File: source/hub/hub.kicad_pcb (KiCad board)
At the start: 2 copper layers, 72 x 15 mm, 18 parts, among them J1 10.0 180° ZCJB-HJ, J2 10.0 180° ZCJB-HJ, J3 918-118A2021Y40002, J4 TYPEC-303-ACP16, U1 SL2.1A, X1 12 MHz

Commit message: finished redesigning
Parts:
- C3: value 10uF -> 10 uF
- moved X1 0.25 mm to (202.7, 100.5)
- moved R2 0.10 mm to (160.3, 106.9)
- renumbered J2 to J1, J3 to J2, J1 to J3
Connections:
- J1 pad 2: /DM2 -> /DM1
- J1 pad 3: /DP2 -> /DP1
- J3 pad 2: /DM1 -> /DM2
- J3 pad 3: /DP1 -> /DP2
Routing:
- net /DP2: track 35.6 -> 15.2 mm, vias 1 -> 0
- net /DM: track 43.1 -> 62.8 mm, vias 0 -> 3
- net /DM3: track 36.6 -> 54.2 mm, vias 1 -> 2
- net /DP1: track 12.1 -> 29.6 mm
- net /DM1: track 14.1 -> 29.8 mm
- net /DP: track 46.3 -> 60.3 mm
- net /DP3: track 40.7 -> 53.0 mm, vias 3 -> 2
- net /DM2: track 25.6 -> 16.7 mm
- net Net-(C7-Pad1): track 21.4 -> 16.1 mm, vias 1 -> 2
- net +5V: track 86.1 -> 84.6 mm, vias 3 -> 4
- net Earth: track 113.2 -> 114.6 mm, vias 0 -> 6
- net Net-(U1-VDD18): track 2.99 -> 3.57 mm
- net Net-(U1-XOUT): track 14.4 -> 13.9 mm, vias 2 -> 0

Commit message: updated missing routes
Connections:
- C7 pad 1: Net-(C7-Pad1) -> +5V
- C8 pad 1: Net-(C7-Pad1) -> +5V
- J2 pad 10: Net-(C7-Pad1) -> +5V
- J2 pad 15: Net-(C7-Pad1) -> +5V
- J2 pad 2: Net-(C7-Pad1) -> +5V
- J2 pad 7: Net-(C7-Pad1) -> +5V
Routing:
- net +5V: track 84.6 -> 114.9 mm, vias 4 -> 7
- net Net-(C7-Pad1): track 16.1 -> 0.00 mm, vias 2 -> 0

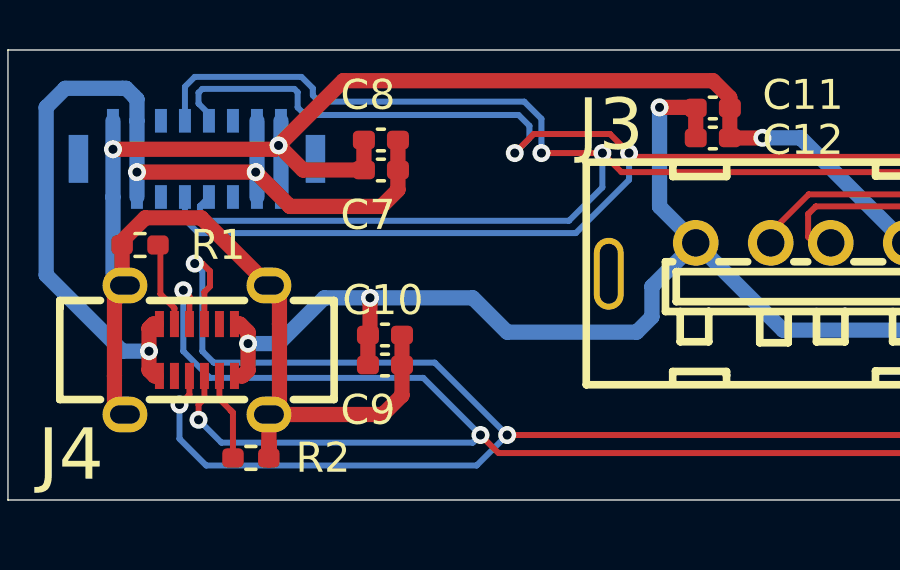
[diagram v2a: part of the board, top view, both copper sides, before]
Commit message: add name and contact
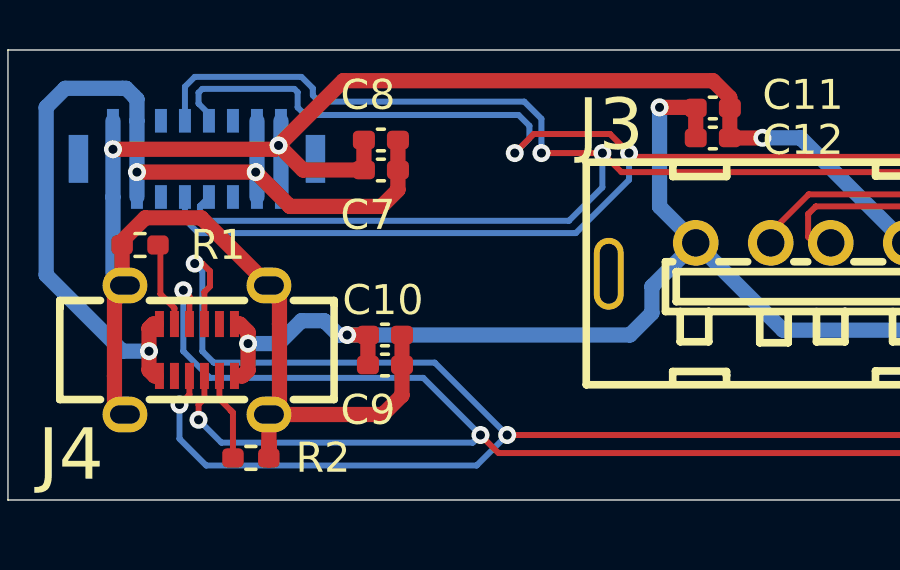
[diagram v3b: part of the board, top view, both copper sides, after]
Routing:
- net +5V: track 114.9 -> 113.7 mm
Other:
- board text added: "Designed By Ethan Hu 4/14/2025"
- board text added: "Email: ethanhu8351@gmail.com Github: PythonOrC"
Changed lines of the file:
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@@
 		(layer "Edge.Cuts")
+	)
+	(gr_text "Designed By Ethan Hu 4/14/2025"
+		(at 222.283075 97.2231 0)
+		(layer "B.SilkS")
+		(effects
+			(font
+				(size 1.5 1.5)
+				(thickness 0.3)
+				(bold yes)
+			)
+			(justify left bottom mirror)
+		)
+	)
+	(gr_text "Email: ethanhu8351@gmail.com\nGithub: PythonOrC"
+		(at 222.283075 106.3671 0)
+		(layer "B.SilkS")
+		(effects
+			(font
+				(size 1.143 1.143)
+				(thickness 0.2286)
+				(bold yes)
+			)
+			(justify left bottom mirror)
+		)
 	)
 	(segment
@@
 	)
 	(segment
-		(start 164.244075 101.5411)
-		(end 164.244075 102.711125)
-		(width 0.508)
-		(layer "F.Cu")
-		(net 2)
-	)
-	(segment
 		(start 160.180075 103.0651)
 		(end 160.180075 102.6841)
@@
 	)
 	(segment
-		(start 164.244075 102.711125)
-		(end 164.1761 102.7791)
-		(width 0.508)
-		(layer "F.Cu")
-		(net 2)
-	)
-	(segment
 		(start 159.989955 104.14422)
 		(end 159.83016 104.14422)
@@
 	)
 	(segment
+		(start 163.482075 102.7791)
+		(end 164.1761 102.7791)
+		(width 0.508)
+		(layer "F.Cu")
+		(net 2)
+	)
+	(segment
 		(start 198.788075 106.7481)
 		(end 198.788075 103.1921)
@@
 	)
 	(via
-		(at 164.244075 101.5411)
+		(at 163.482075 102.7791)
 		(size 0.6)
 		(drill 0.3)
@@
 	)
 	(segment
+		(start 161.196075 103.0651)
+		(end 160.180075 103.0651)
+		(width 0.508)
+		(layer "B.Cu")
+		(net 2)
+	)
+	(segment
 		(start 156.370075 94.8101)
 		(end 156.116075 94.5561)
@@
 	)
 	(segment
+		(start 163.482075 102.7791)
+		(end 172.912075 102.7791)
+		(width 0.508)
+		(layer "B.Cu")
+		(net 2)
+	)
+	(segment
 		(start 154.084075 94.5561)
 		(end 153.449075 95.1911)
@@
 	)
 	(segment
+		(start 162.720075 102.3031)
+		(end 161.958075 102.3031)
+		(width 0.508)
+		(layer "B.Cu")
+		(net 2)
+	)
+	(segment
+		(start 173.642075 101.1601)
+		(end 175.094215 99.70796)
+		(width 0.508)
+		(layer "B.Cu")
+		(net 2)
+	)
+	(segment
+		(start 172.912075 102.7791)
+		(end 173.642075 102.0491)
+		(width 0.508)
+		(layer "B.Cu")
+		(net 2)
+	)
+	(segment
+		(start 173.896075 98.5009)
+		(end 173.896075 95.1911)
+		(width 0.508)
+		(layer "B.Cu")
+		(net 2)
+	)
+	(segment
+		(start 178.011875 102.6167)
+		(end 175.103135 99.70796)
+		(width 0.508)
+		(layer "B.Cu")
+		(net 2)
+	)
+	(segment
+		(start 156.878075 103.3191)
+		(end 155.989075 103.3191)
+		(width 0.508)
+		(layer "B.Cu")
+		(net 2)
+	)
+	(segment
+		(start 153.449075 95.1911)
+		(end 153.449075 100.7791)
+		(width 0.508)
+		(layer "B.Cu")
+		(net 2)
+	)
+	(segment
+		(start 156.116075 94.5561)
+		(end 155.989075 94.5561)
+		(width 0.508)
+		(layer "B.Cu")
+		(net 2)
+	)
+	(segment
+		(start 173.642075 102.0491)
+		(end 173.642075 101.1601)
+		(width 0.508)
+		(layer "B.Cu")
+		(net 2)
+	)
+	(segment
+		(start 175.103135 99.70796)
+		(end 173.896075 98.5009)
+		(width 0.508)
+		(layer "B.Cu")
+		(net 2)
+	)
+	(segment
+		(start 155.989075 103.3191)
+		(end 153.449075 100.7791)
+		(width 0.508)
+		(layer "B.Cu")
+		(net 2)
+	)
+	(segment
 		(start 175.094215 99.70796)
 		(end 175.103135 99.70796)
@@
 	)
 	(segment
-		(start 168.816075 102.6841)
-		(end 173.134075 102.6841)
-		(width 0.508)
-		(layer "B.Cu")
-		(net 2)
-	)
-	(segment
-		(start 173.896075 98.5009)
-		(end 173.896075 95.1911)
-		(width 0.508)
-		(layer "B.Cu")
-		(net 2)
-	)
-	(segment
-		(start 173.642075 102.1761)
-		(end 173.642075 101.1601)
-		(width 0.508)
-		(layer "B.Cu")
-		(net 2)
-	)
-	(segment
-		(start 178.011875 102.6167)
-		(end 175.103135 99.70796)
-		(width 0.508)
-		(layer "B.Cu")
-		(net 2)
-	)
-	(segment
-		(start 156.878075 103.3191)
-		(end 155.989075 103.3191)
-		(width 0.508)
-		(layer "B.Cu")
-		(net 2)
-	)
-	(segment
-		(start 153.449075 95.1911)
-		(end 153.449075 100.7791)
-		(width 0.508)
-		(layer "B.Cu")
-		(net 2)
-	)
-	(segment
-		(start 156.116075 94.5561)
-		(end 155.989075 94.5561)
-		(width 0.508)
-		(layer "B.Cu")
-		(net 2)
-	)
-	(segment
-		(start 175.103135 99.70796)
-		(end 173.896075 98.5009)
-		(width 0.508)
-		(layer "B.Cu")
-		(net 2)
-	)
-	(segment
-		(start 155.989075 103.3191)
-		(end 153.449075 100.7791)
-		(width 0.508)
-		(layer "B.Cu")
-		(net 2)
-	)
-	(segment
-		(start 164.244075 101.5411)
-		(end 167.673075 101.5411)
-		(width 0.508)
-		(layer "B.Cu")
-		(net 2)
-	)
-	(segment
-		(start 173.134075 102.6841)
-		(end 173.642075 102.1761)
+		(start 161.958075 102.3031)
+		(end 161.196075 103.0651)
 		(width 0.508)
 		(layer "B.Cu")
@@
 	)
 	(segment
-		(start 167.673075 101.5411)
-		(end 168.816075 102.6841)
-		(width 0.508)
-		(layer "B.Cu")
-		(net 2)
-	)
-	(segment
-		(start 160.180075 103.0651)
-		(end 161.196075 103.0651)
+		(start 163.482075 102.7791)
+		(end 163.196075 102.7791)
+		(width 0.508)
+		(layer "B.Cu")
+		(net 2)
+	)
+	(segment
+		(start 163.196075 102.7791)
+		(end 162.720075 102.3031)
 		(width 0.508)
 		(layer "B.Cu")
@@
 	)
 	(segment
-		(start 173.642075 101.1601)
-		(end 175.094215 99.70796)
-		(width 0.508)
-		(layer "B.Cu")
-		(net 2)
-	)
-	(segment
 		(start 155.989075 94.5561)
 		(end 154.084075 94.5561)
@@
 		(width 0.508)
 		(layer "B.Cu")
-		(net 2)
-	)
-	(segment
-		(start 161.196075 103.0651)
-		(end 162.720075 101.5411)
-		(width 0.508)
-		(layer "B.Cu")
-		(net 2)
-	)
-	(segment
-		(start 162.720075 101.5411)
-		(end 164.244075 101.5411)
-		(width 0.508)
-		(layer "B.Cu")

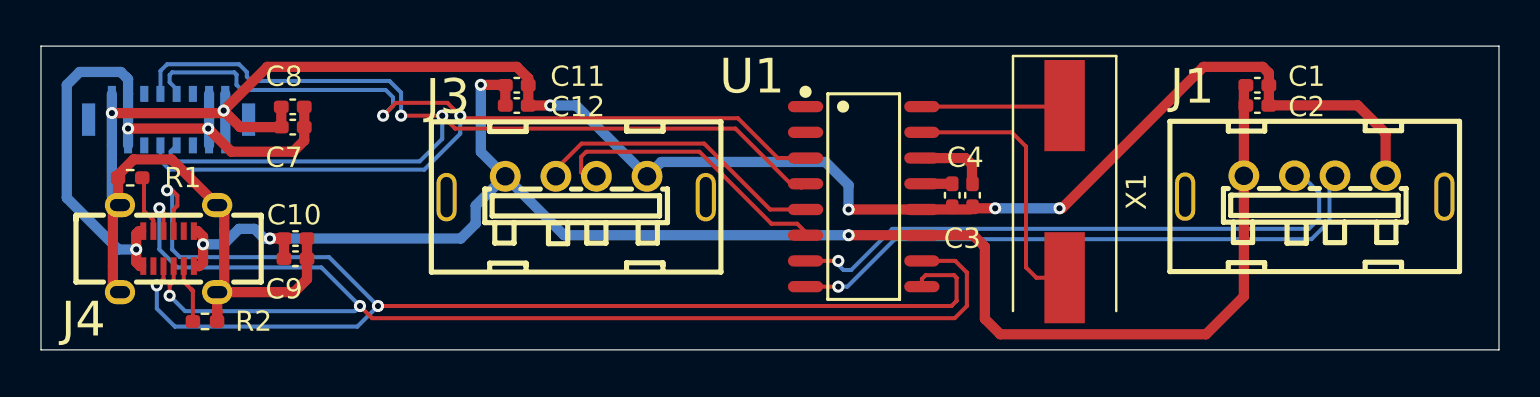
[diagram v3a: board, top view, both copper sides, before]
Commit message: add copper zone
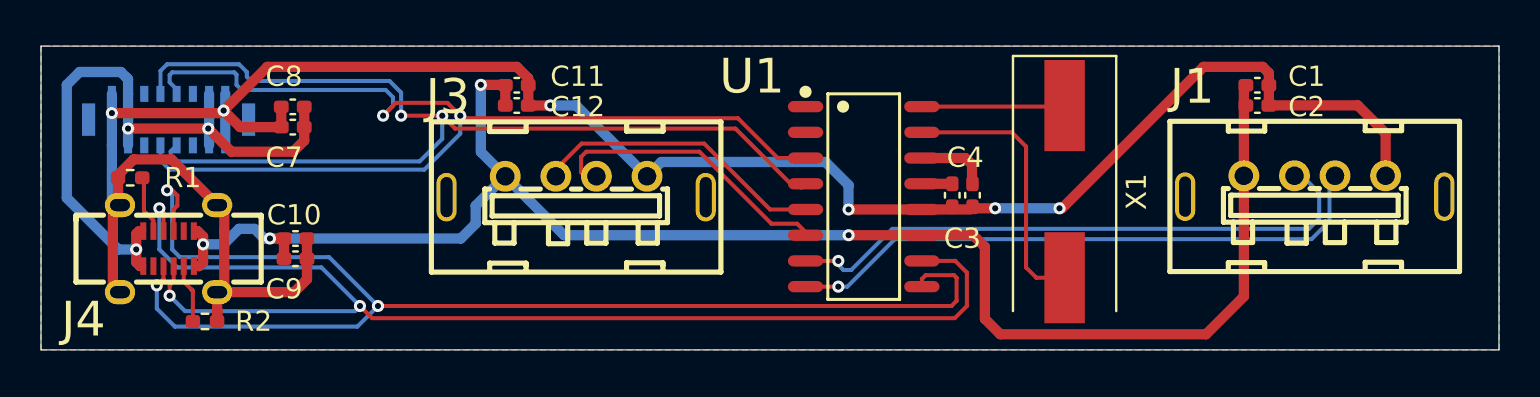
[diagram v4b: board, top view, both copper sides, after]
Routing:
- added copper zone on B.Cu, net Earth
- added copper zone on F.Cu, net Earth
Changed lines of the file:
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@@
 	(net 30 "unconnected-(U1-DP4-Pad2)")
 	(footprint "Capacitor_SMD:C_0402_1005Metric_Pad0.74x0.62mm_HandSolder"
-		(placed yes)
 		(layer "F.Cu")
 		(at 212.243575 96.2117)
@@
 	)
 	(footprint "Capacitor_SMD:C_0402_1005Metric_Pad0.74x0.62mm_HandSolder"
-		(placed yes)
 		(layer "F.Cu")
 		(at 164.7436 102.7791)
@@
 	)
 	(footprint "Capacitor_SMD:C_0402_1005Metric_Pad0.74x0.62mm_HandSolder"
-		(placed yes)
 		(layer "F.Cu")
 		(at 164.7436 103.7791)
@@
 	)
 	(footprint "Capacitor_SMD:C_0402_1005Metric_Pad0.74x0.62mm_HandSolder"
-		(placed yes)
 		(layer "F.Cu")
 		(at 175.671575 96.2117)
@@
 	)
 	(footprint "Capacitor_SMD:C_0402_1005Metric_Pad0.74x0.62mm_HandSolder"
-		(placed yes)
 		(layer "F.Cu")
 		(at 212.243575 95.2117)
@@
 	)
 	(footprint "Resistor_SMD:R_0402_1005Metric_Pad0.72x0.64mm_HandSolder"
-		(placed yes)
 		(layer "F.Cu")
 		(at 156.5786 99.7791)
@@
 	)
 	(footprint "Capacitor_SMD:C_0402_1005Metric_Pad0.74x0.62mm_HandSolder"
-		(placed yes)
 		(layer "F.Cu")
 		(at 197.176075 100.6442 -90)
@@
 	)
 	(footprint "custom-components:USB-C-SMD_TYPEC-303-ACP16"
-		(placed yes)
 		(layer "F.Cu")
 		(at 158.4761 103.2791)
@@
 			(drill oval 1 0.6096)
 			(layers "*.Cu" "*.Mask")
-			(remove_unused_layers yes)
-			(keep_end_layers yes)
-			(zone_layer_connections)
+			(remove_unused_layers no)
 			(net 1 "Earth")
 			(pinfunction "GND")
@@
 			(drill oval 1 0.6096)
 			(layers "*.Cu" "*.Mask")
-			(remove_unused_layers yes)
-			(keep_end_layers yes)
-			(zone_layer_connections)
+			(remove_unused_layers no)
 			(net 1 "Earth")
 			(pinfunction "GND")
@@
 			)
 			(layers "*.Cu" "*.Mask")
-			(remove_unused_layers yes)
-			(keep_end_layers yes)
-			(zone_layer_connections)
+			(remove_unused_layers no)
 			(net 1 "Earth")
 			(pinfunction "GND")
@@
 			(drill oval 1 0.6096)
 			(layers "*.Cu" "*.Mask")
-			(remove_unused_layers yes)
-			(keep_end_layers yes)
-			(zone_layer_connections)
+			(remove_unused_layers no)
 			(net 1 "Earth")
 			(pinfunction "GND")
@@
 	)
 	(footprint "Capacitor_SMD:C_0402_1005Metric_Pad0.74x0.62mm_HandSolder"
-		(placed yes)
 		(layer "F.Cu")
 		(at 198.176075 100.6442 -90)
@@
 	)
 	(footprint "Resistor_SMD:R_0402_1005Metric_Pad0.72x0.64mm_HandSolder"
-		(placed yes)
 		(layer "F.Cu")
 		(at 160.2736 106.8751 180)
@@
 	)
 	(footprint "Capacitor_SMD:C_0402_1005Metric_Pad0.74x0.62mm_HandSolder"
-		(placed yes)
 		(layer "F.Cu")
 		(at 175.671575 95.2117)
@@
 	)
 	(footprint "custom-components:SOP-16_L10.0-W3.9-P1.27-LS6.0-BL"
-		(placed yes)
 		(layer "F.Cu")
 		(at 192.803575 100.7117 -90)
@@
 		)
 		(embedded_fonts no)
+		(model "D:/KiCad/8.0/share/kicad/3dmodels/Package_SO.3dshapes/SOP-16_3.9x9.9mm_P1.27mm.step"
+			(offset
+				(xyz 0 0 0)
+			)
+			(scale
+				(xyz 1 1 1)
+			)
+			(rotate
+				(xyz -0 -0 -90)
+			)
+		)
 	)
 	(footprint "custom-components:USB-A-FEMALE"
-		(placed yes)
 		(layer "F.Cu")
 		(at 178.603275 100.223)
@@
 			)
 			(layers "*.Cu" "*.Mask")
-			(remove_unused_layers yes)
-			(keep_end_layers yes)
-			(zone_layer_connections)
+			(remove_unused_layers no)
 			(net 2 "+5V")
 			(pinfunction "VCC")
@@
 			)
 			(layers "*.Cu" "*.Mask")
-			(remove_unused_layers yes)
-			(keep_end_layers yes)
-			(zone_layer_connections)
+			(remove_unused_layers no)
 			(net 11 "/DM2")
 			(pinfunction "D-")
@@
 			)
 			(layers "*.Cu" "*.Mask")
-			(remove_unused_layers yes)
-			(keep_end_layers yes)
-			(zone_layer_connections)
+			(remove_unused_layers no)
 			(net 12 "/DP2")
 			(pinfunction "D+")
@@
 			)
 			(layers "*.Cu" "*.Mask")
-			(remove_unused_layers yes)
-			(keep_end_layers yes)
-			(zone_layer_connections)
+			(remove_unused_layers no)
 			(net 1 "Earth")
 			(pinfunction "GND")
@@
 			)
 			(layers "*.Cu" "*.Mask")
-			(remove_unused_layers yes)
-			(keep_end_layers yes)
-			(zone_layer_connections)
+			(remove_unused_layers no)
 			(net 19 "unconnected-(J3-EH-Pad5)")
 			(pinfunction "EH")
@@
 			)
 			(layers "*.Cu" "*.Mask")
-			(remove_unused_layers yes)
-			(keep_end_layers yes)
-			(zone_layer_connections)
+			(remove_unused_layers no)
 			(net 20 "unconnected-(J3-EH-Pad6)")
 			(pinfunction "EH")
@@
 	)
 	(footprint "Capacitor_SMD:C_0402_1005Metric_Pad0.74x0.62mm_HandSolder"
-		(placed yes)
 		(layer "F.Cu")
 		(at 164.6086 97.2791 180)
@@
 	)
 	(footprint "Capacitor_SMD:C_0402_1005Metric_Pad0.74x0.62mm_HandSolder"
-		(placed yes)
 		(layer "F.Cu")
 		(at 164.6086 96.2791 180)
@@
 	)
 	(footprint "custom-components:USB-A-FEMALE"
-		(placed yes)
 		(layer "F.Cu")
 		(at 215.077075 100.1979)
@@
 			)
 			(layers "*.Cu" "*.Mask")
-			(remove_unused_layers yes)
-			(keep_end_layers yes)
-			(zone_layer_connections)
+			(remove_unused_layers no)
 			(net 2 "+5V")
 			(pinfunction "VCC")
@@
 			)
 			(layers "*.Cu" "*.Mask")
-			(remove_unused_layers yes)
-			(keep_end_layers yes)
-			(zone_layer_connections)
+			(remove_unused_layers no)
 			(net 7 "/DM1")
 			(pinfunction "D-")
@@
 			)
 			(layers "*.Cu" "*.Mask")
-			(remove_unused_layers yes)
-			(keep_end_layers yes)
-			(zone_layer_connections)
+			(remove_unused_layers no)
 			(net 8 "/DP1")
 			(pinfunction "D+")
@@
 			)
 			(layers "*.Cu" "*.Mask")
-			(remove_unused_layers yes)
-			(keep_end_layers yes)
-			(zone_layer_connections)
+			(remove_unused_layers no)
 			(net 1 "Earth")
 			(pinfunction "GND")
@@
 			)
 			(layers "*.Cu" "*.Mask")
-			(remove_unused_layers yes)
-			(keep_end_layers yes)
-			(zone_layer_connections)
+			(remove_unused_layers no)
 			(net 5 "unconnected-(J1-EH-Pad5)")
 			(pinfunction "EH")
@@
 			)
 			(layers "*.Cu" "*.Mask")
-			(remove_unused_layers yes)
-			(keep_end_layers yes)
-			(zone_layer_connections)
+			(remove_unused_layers no)
 			(net 6 "unconnected-(J1-EH-Pad6)")
 			(pinfunction "EH")
@@
 	)
 	(footprint "custom-components:TYPE-C-SMD-MALE"
-		(placed yes)
 		(layer "B.Cu")
 		(at 158.4761 96.9091)
@@
 		)
 		(embedded_fonts no)
+		(model "${KICAD9_3DMODEL_DIR}/Connector_USB.3dshapes/USB_C_Plug_ShenzhenJingTuoJin_918-118A2021Y40002_Vertical.wrl"
+			(offset
+				(xyz 0 0 0)
+			)
+			(scale
+				(xyz 1 1 1)
+			)
+			(rotate
+				(xyz -0 -0 -90)
+			)
+		)
 	)
 	(gr_rect
@@
 		(net 29)
 	)
+	(zone
+		(net 1)
+		(net_name "Earth")
+		(layers "F.Cu" "B.Cu")
+		(hatch edge 0.5)
+		(connect_pads
+			(clearance 0.5)
+		)
+		(min_thickness 0.25)
+		(filled_areas_thickness no)
+		(fill yes
+			(thermal_gap 0.5)
+			(thermal_bridge_width 0.5)
+		)
+		(polygon
+			(pts
+				(xy 152.179075 93.2861) (xy 152.179075 108.2721) (xy 224.188075 108.2721) (xy 224.188075 93.2861)
+			)
+		)
+	)
 	(embedded_fonts no)

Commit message: added gnd vias copper pour
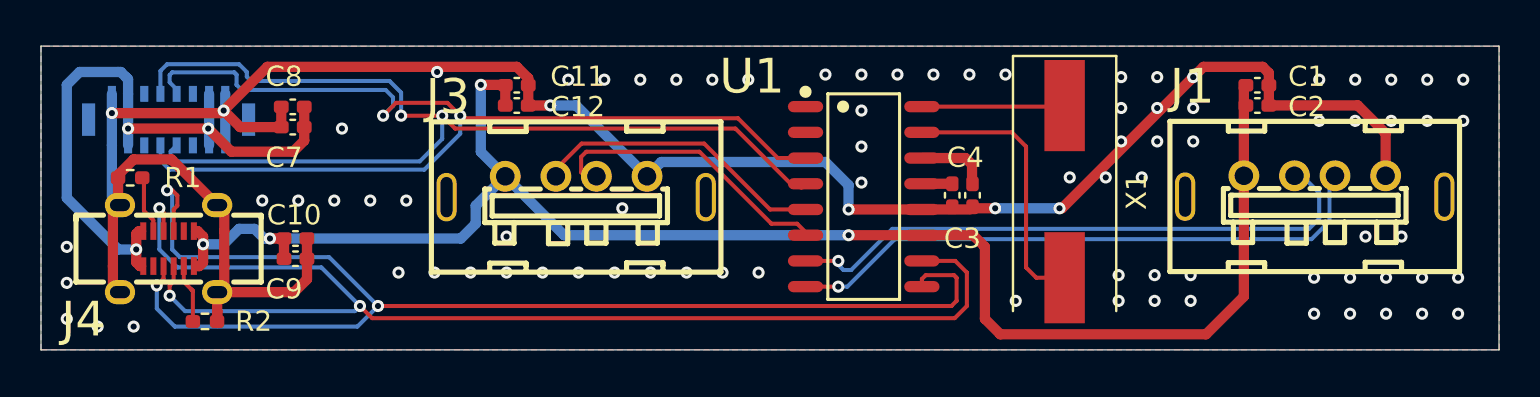
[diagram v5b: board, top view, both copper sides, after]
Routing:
- net Earth: vias 6 -> 87
